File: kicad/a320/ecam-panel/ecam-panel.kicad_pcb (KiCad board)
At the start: 2 copper layers, 61 parts, among them P1 CONN_02X04, P2 CONN_01X03, P3 CONN_01X03, P4 CONN_02X05, P5 CONN_02X05, SW1 SW_PUSH_SMALL, SW10 SW_PUSH_SMALL, SW11 SW_PUSH_SMALL, SW12 SW_PUSH_SMALL, SW13 SW_PUSH_SMALL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

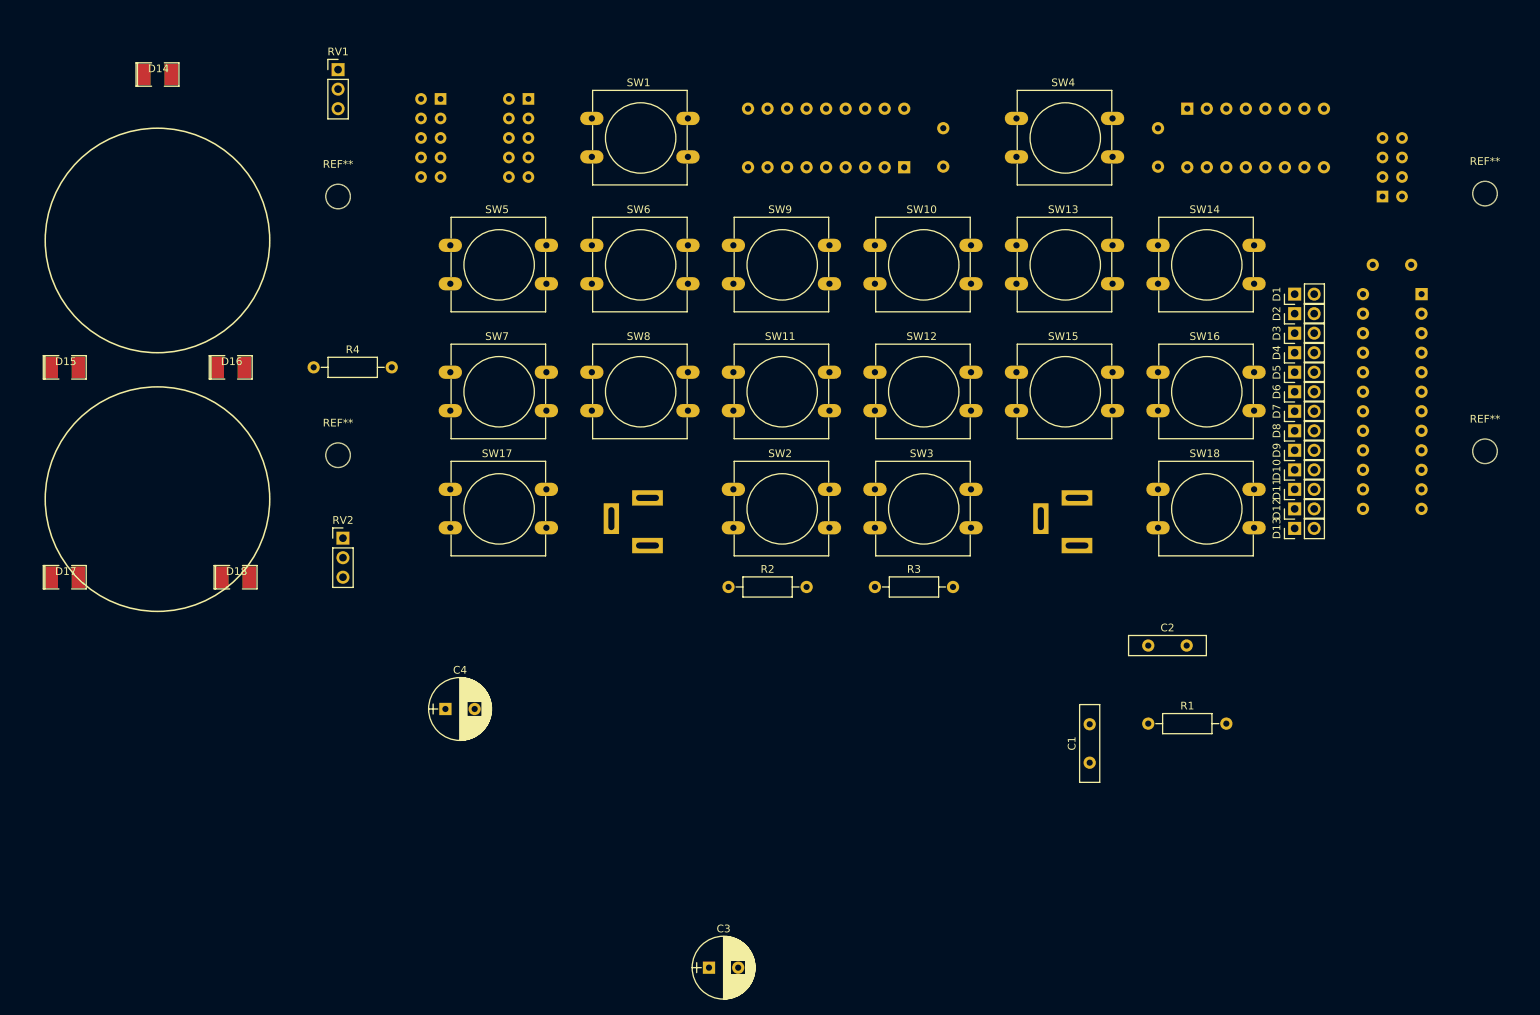
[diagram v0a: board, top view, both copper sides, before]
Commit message: Adjust footprints layout in A320 ECAM panel
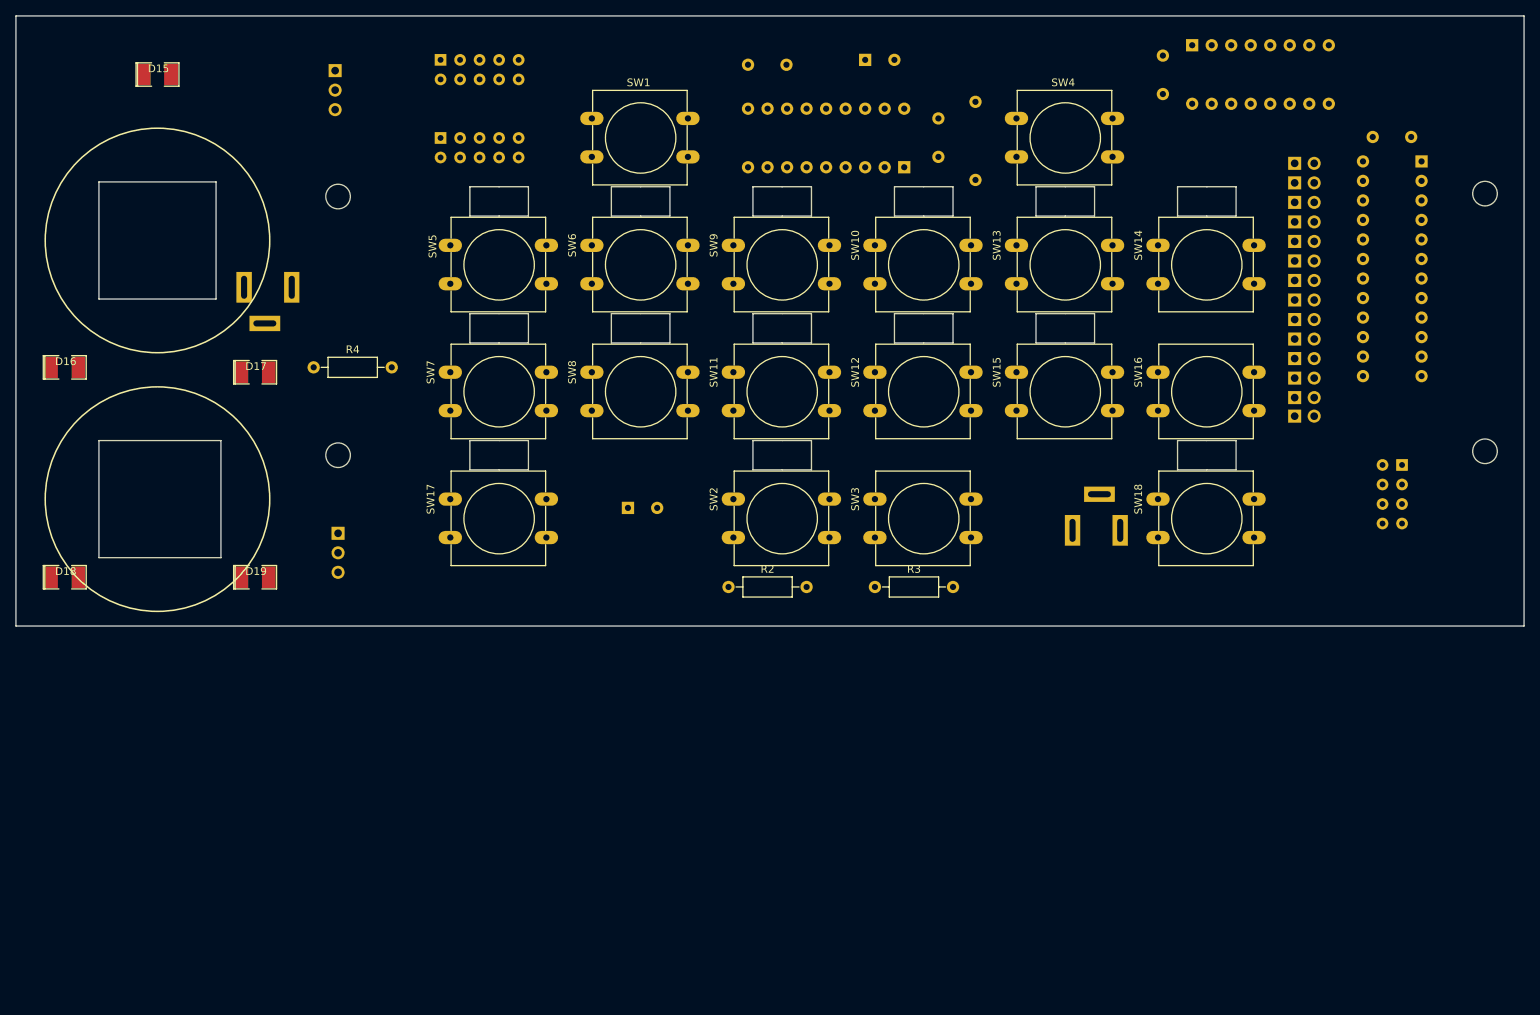
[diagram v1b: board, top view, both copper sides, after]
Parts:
- removed C7: 100nF, avionica:Disc_capacitor
- added D14: Led_Small, avionica:Pin_Header_1x02, B.Cu at (197.5, 90.2)
- C1, C3, D1, D10, D11, D12, D13, D2, D3, D4, D5, D6, D7, D8, D9, R1, RV1, RV2: moved to B.Cu
- C2: value 100nF -> 1uF; footprint avionica:Disc_capacitor -> avionica:Radial_capacitor; moved to B.Cu
- C4: value 1uF -> 100nF; footprint avionica:Radial_capacitor -> avionica:Disc_capacitor; moved to B.Cu
- moved C4 141.8 mm to (207.6, 53.8)
- moved P3 104.1 mm to (63.5, 78.1), turned to 180 degrees
- moved C1 101.1 mm to (126.4, 44.5), turned to 0 degrees
- moved C2 84.6 mm to (141.6, 43.8)
- moved R1 74.2 mm to (156.0, 59.4), turned to 90 degrees
- moved P2 63.6 mm to (172.1, 100.3), turned to 0 degrees
- moved C3 60.7 mm to (110.7, 102.1)
- moved D13 47.5 mm to (197.5, 57.3), turned to 270 degrees
- moved D12 42.4 mm to (197.5, 59.8), turned to 270 degrees
- moved D11 37.3 mm to (197.5, 62.4), turned to 270 degrees
- moved P1 35.0 mm to (211.5, 96.5), turned to 180 degrees
- moved D10 32.3 mm to (197.5, 64.9), turned to 270 degrees
- moved C6 28.9 mm to (180.3, 48.3), turned to 90 degrees
- moved C5 28.6 mm to (151.1, 51.4)
- moved D9 27.2 mm to (197.5, 67.4), turned to 270 degrees
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- renumbered D14 to D15, D15 to D16, D16 to D17, D17 to D18, D18 to D19
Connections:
- C1 pad 1: VCC -> Net-(C1-Pad1)
- C3 pad 1: Net-(C3-Pad1) -> L1
- C4 pad 1: L1 -> VCC
- P5 pad 10: Net-(P5-Pad10) -> (no net)
- P5 pad 9: Net-(P5-Pad9) -> (no net)
- U1 pad 12: Net-(U1-Pad12) -> (no net)
- U1 pad 2: Net-(U1-Pad2) -> (no net)
- U2 pad 5: Net-(C2-Pad1) -> Net-(C1-Pad1)
- U2 pad 6: Net-(C3-Pad1) -> Net-(C2-Pad1)
- U3 pad 10: Net-(U3-Pad10) -> (no net)
- U3 pad 24: Net-(U3-Pad24) -> (no net)
- U3 pad 3: Net-(U3-Pad3) -> (no net)
- U3 pad 5: Net-(U3-Pad5) -> (no net)
- U3 pad 6: Net-(U3-Pad6) -> (no net)
- U3 pad 7: Net-(U3-Pad7) -> (no net)
- U3 pad 8: Net-(U3-Pad8) -> (no net)
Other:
- board outline added: 196.2 x 79.4 mm

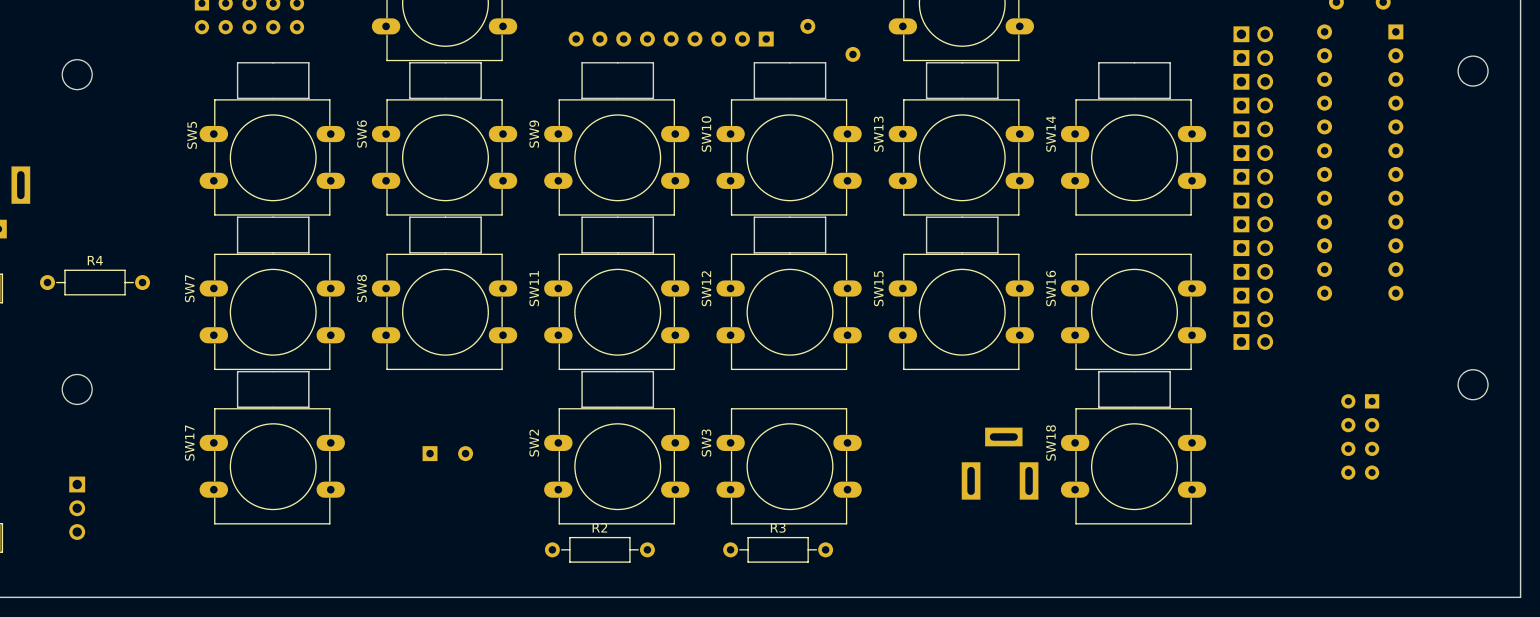
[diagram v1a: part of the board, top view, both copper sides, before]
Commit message: Make some final adjustments on footprints for A320 ECAM panel
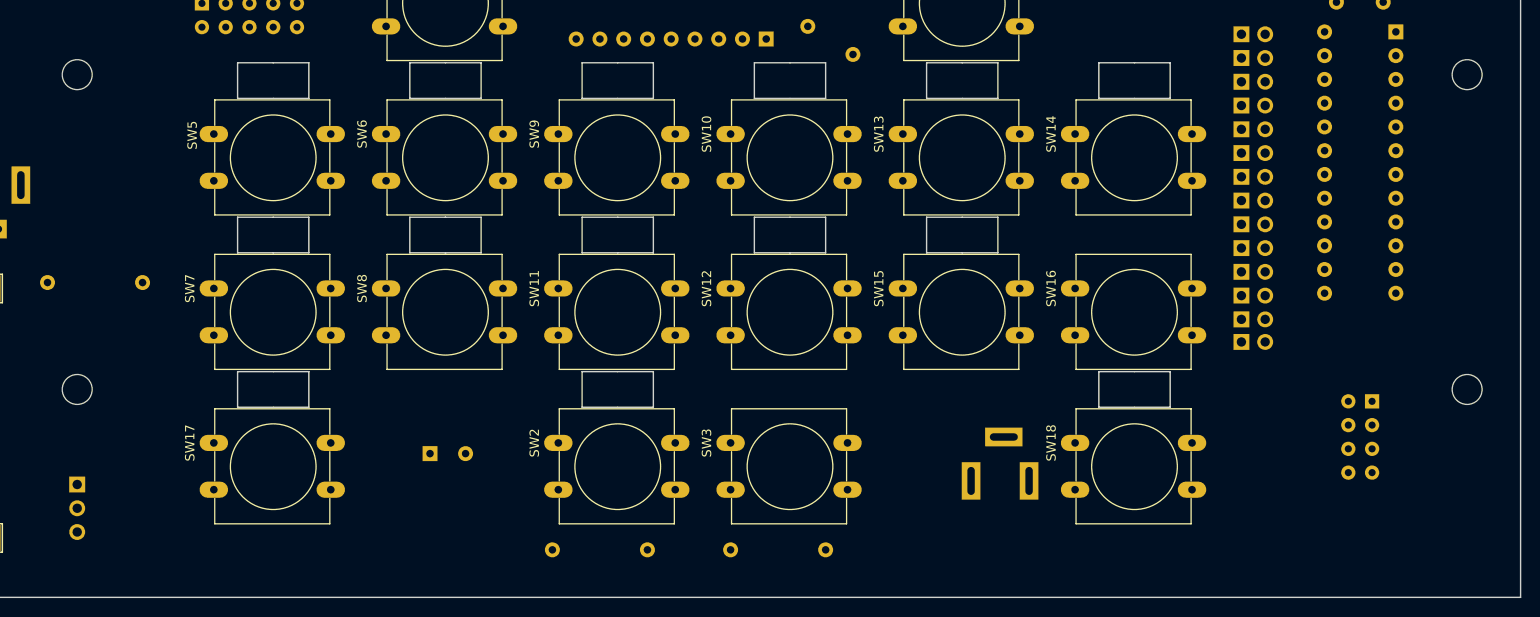
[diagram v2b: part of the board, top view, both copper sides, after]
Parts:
- R2, R3, R4: moved to B.Cu
- moved REF** 0.81 mm to (221.6, 95.2)
- moved REF** 0.74 mm to (221.6, 61.6)

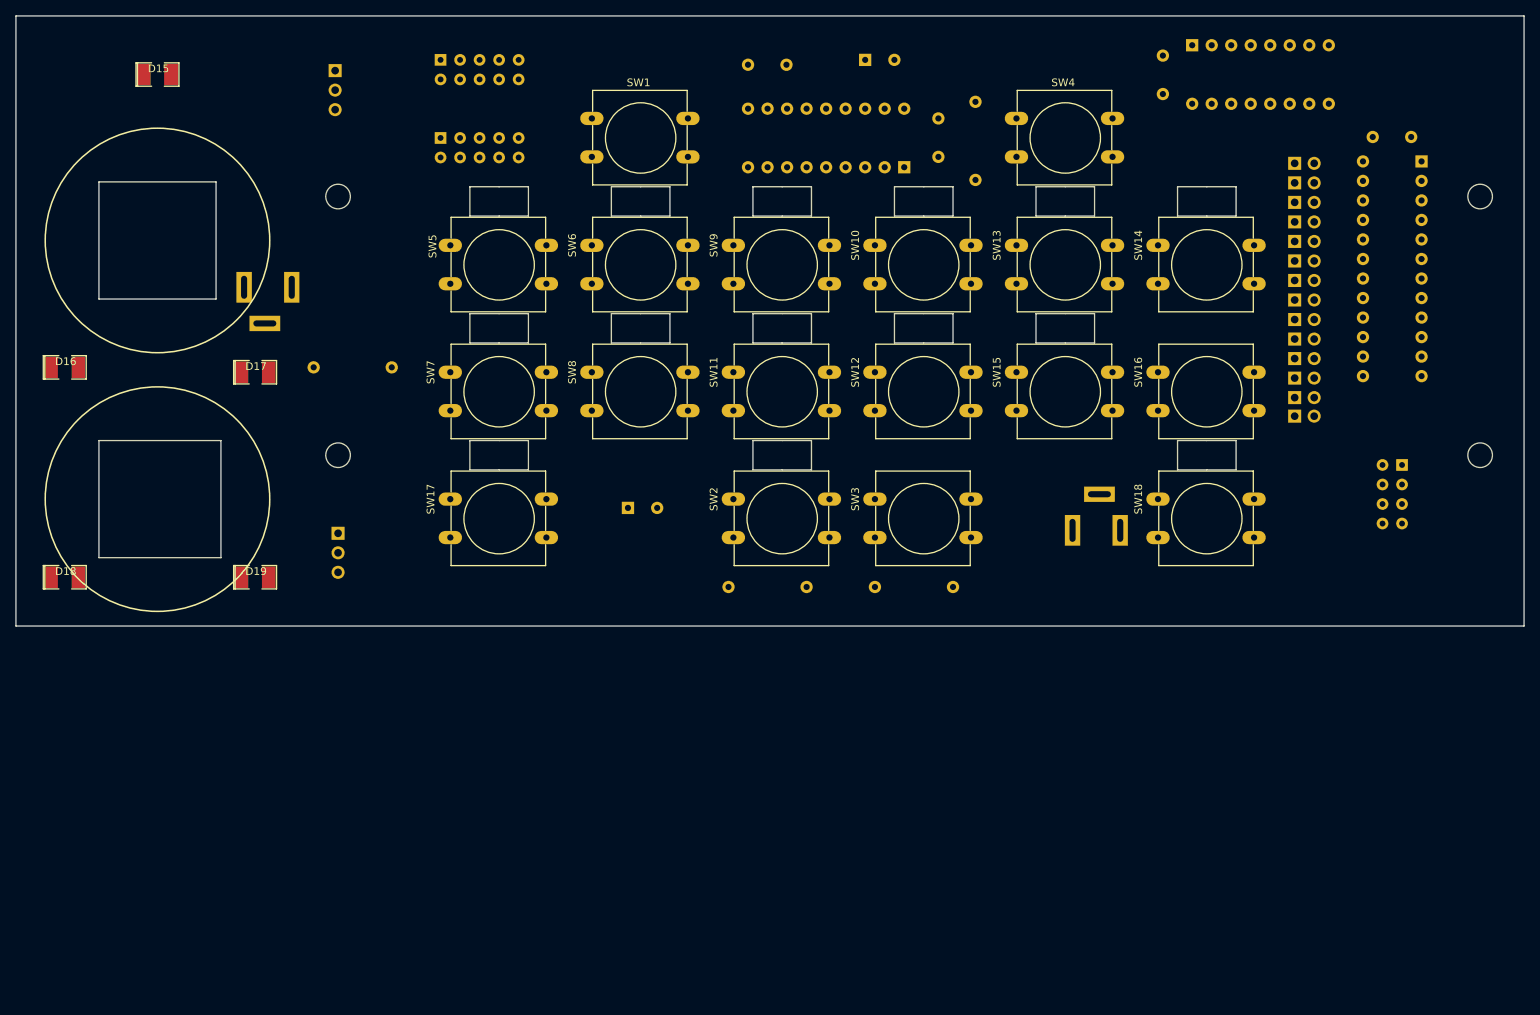
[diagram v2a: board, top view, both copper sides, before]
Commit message: Complete the tracks of the PCB in A320 ECAM panel
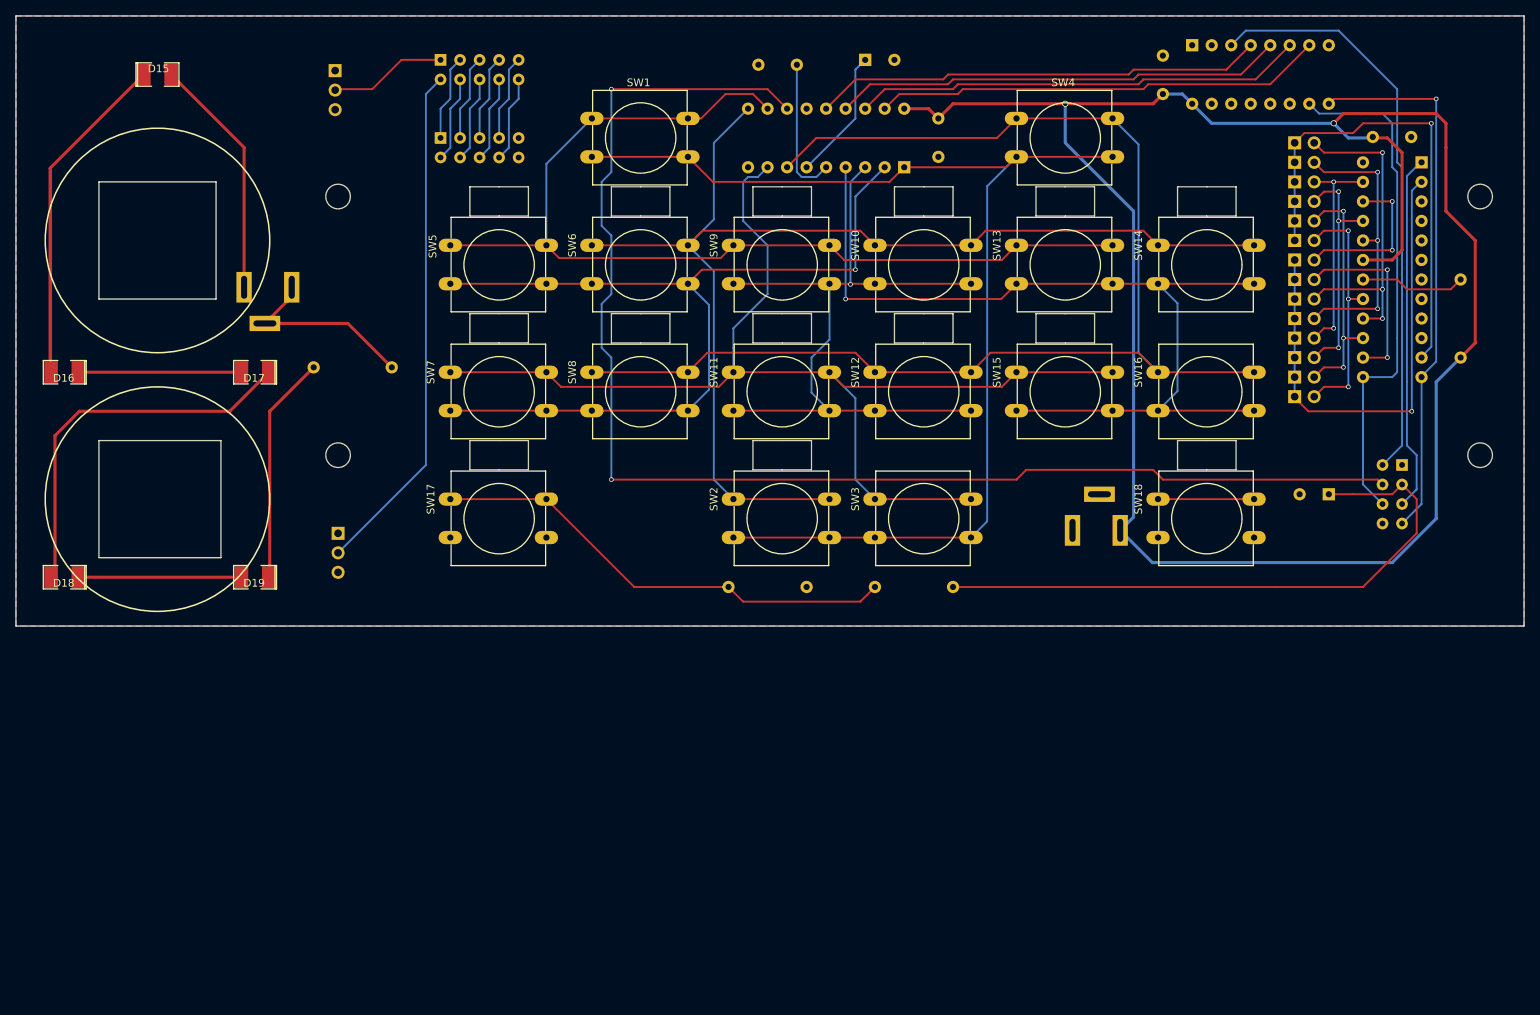
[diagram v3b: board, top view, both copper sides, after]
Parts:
- D1, D10, D11, D12, D13, D14, D2, D3, D4, D5, D6, D7, D8, D9: value Led_Small -> (none)
- moved C3 91.2 mm to (201.9, 100.3), turned to 180 degrees
- moved R1 67.2 mm to (219.1, 82.5)
- moved D14 35.6 mm to (197.5, 54.6)
- moved R3 10.2 mm to (153.0, 112.4), turned to 180 degrees
- moved C1 6.35 mm to (132.7, 44.5), turned to 180 degrees
- moved D16 0.64 mm to (37.5, 84.5), turned to 180 degrees
- moved D1 0.13 mm to (197.5, 87.6)
- moved D10 0.13 mm to (197.5, 64.8)
- moved D3 0.13 mm to (197.5, 82.5)
- moved D8 0.13 mm to (197.5, 69.8)
- moved D11 0.13 mm to (197.5, 62.2)
- moved D12 0.13 mm to (197.5, 59.7)
- moved D13 0.13 mm to (197.5, 57.1)
- moved D2 0.13 mm to (197.5, 85.1)
- moved D4 0.13 mm to (197.5, 80.0)
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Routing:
- net VCC: track 0.00 -> 264.1 mm, vias 0 -> 2
- net L2: track 0.00 -> 178.5 mm, vias 0 -> 2
- net X4: track 0.00 -> 170.8 mm
- net X2: track 0.00 -> 158.3 mm
- net Y1: track 0.00 -> 153.3 mm
- net X3: track 0.00 -> 152.7 mm
- net X1: track 0.00 -> 133.0 mm
- net Y4: track 0.00 -> 120.6 mm, vias 0 -> 1
- net Y2: track 0.00 -> 118.1 mm, vias 0 -> 1
- net Net-(D17-Pad1): track 0.00 -> 99.0 mm
- net Y3: track 0.00 -> 96.5 mm, vias 0 -> 1
- net Net-(D15-Pad1): track 0.00 -> 87.6 mm
- net L1: track 0.00 -> 80.4 mm
- net L0: track 0.00 -> 75.7 mm
- net Net-(R2-Pad1): track 0.00 -> 74.1 mm
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- added copper zone on B.Cu, net GND
- added copper zone on F.Cu, net GND
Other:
- net class Power added: clearance 0.3, trace_width 0.4, via_dia 0.8, via_drill 0.6
